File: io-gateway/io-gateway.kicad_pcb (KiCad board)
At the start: 4 copper layers, 155 x 81.5 mm, 117 parts, among them IC1 MAX17673AATI+, J1 1752201, J2 1752201, J3 1752201, J4 Screw_Terminal_01x09, J5 Screw_Terminal_01x09, J6 Screw_Terminal_01x09, K1 2071556-2, K2 2071556-2, K3 2071556-2, K4 2071556-2, K5 2071556-2, K6 2071556-2, K7 2071556-2, K9 2071556-2, Q1 NTR4003NT1G, Q2 NTR4003NT1G, Q3 NTR4003NT1G, Q4 NTR4003NT1G, Q5 NTR4003NT1G, Q6 NTR4003NT1G, Q7 NTR4003NT1G, Q9 NTR4003NT1G, U1 LED5000, U2 LED5000

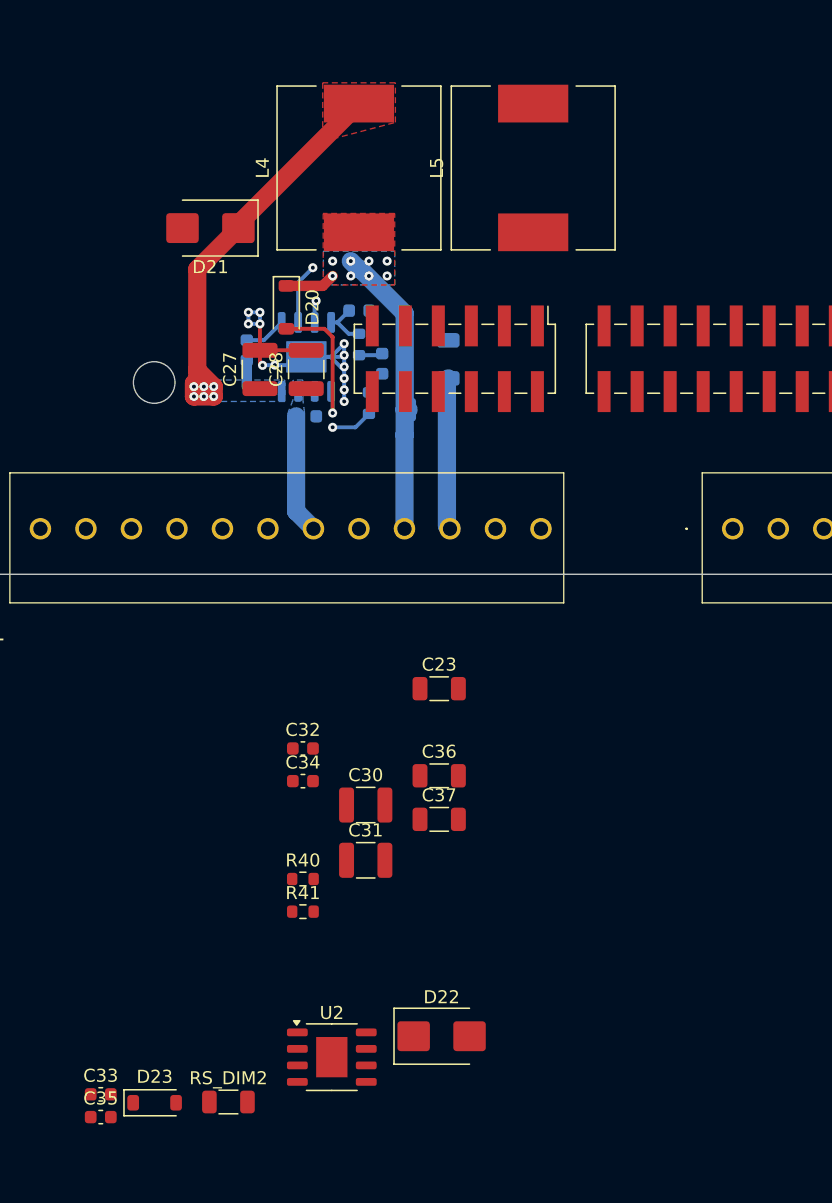
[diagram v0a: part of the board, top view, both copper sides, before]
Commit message: add second dimmer
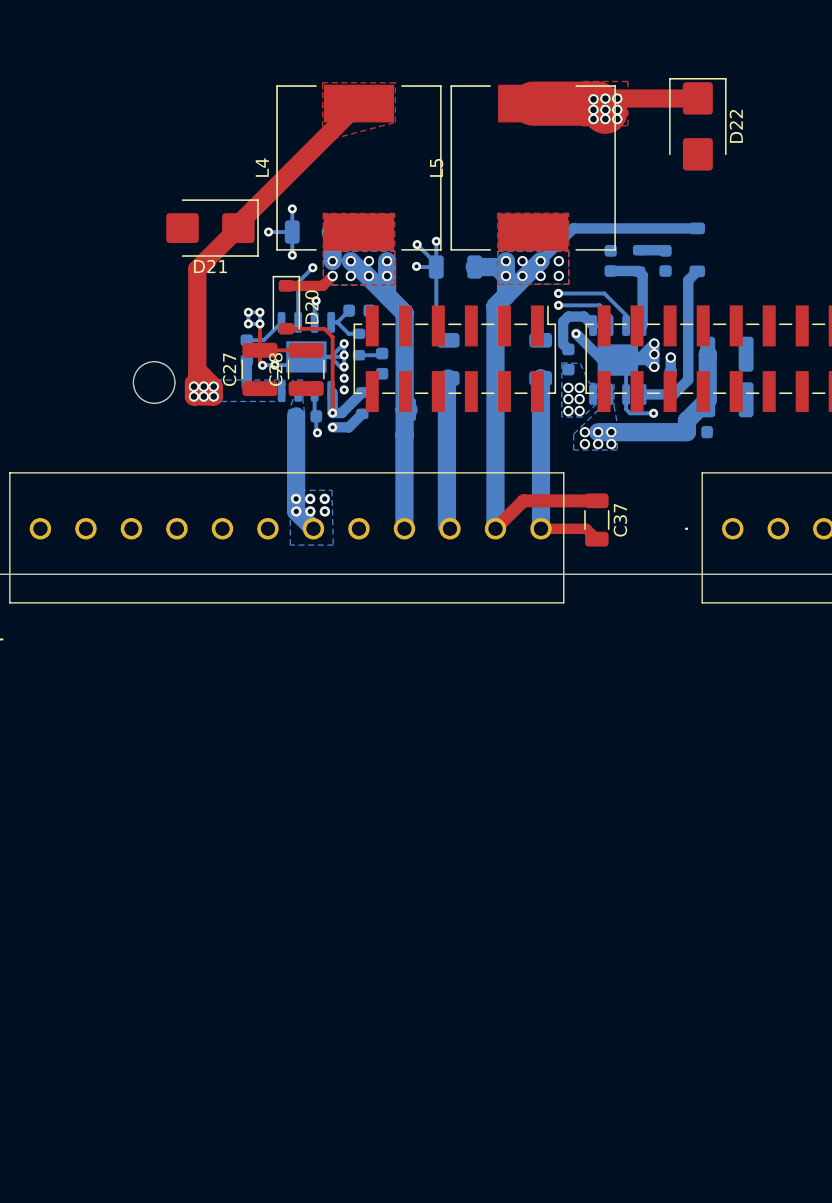
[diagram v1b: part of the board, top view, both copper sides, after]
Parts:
- C23, C30, C31, C32, C33, C34, C35, C36, D23, R40, R41, RS_DIM2, U2: moved to B.Cu
- moved D23 77.7 mm to (105.8, 104.8), turned to -90 degrees
- moved D22 72.7 mm to (105.8, 95.3), turned to -90 degrees
- moved C33 68.5 mm to (105.8, 118.8)
- moved C35 68.5 mm to (95.9, 113.2), turned to -90 degrees
- moved RS_DIM2 62.0 mm to (93.7, 113.2), turned to 90 degrees
- moved U2 58.0 mm to (99.7, 113.3), turned to -90 degrees
- moved R40 54.1 mm to (101.3, 105.7), turned to -90 degrees
- moved R41 49.5 mm to (103.7, 115.1), turned to -90 degrees
- moved C31 47.8 mm to (108.1, 112.8)
- moved C32 46.7 mm to (103.3, 105.7), turned to -90 degrees
- moved C34 46.5 mm to (99.1, 105.7), turned to 90 degrees
- moved C30 41.8 mm to (108.0, 116.3)
- moved C36 39.1 mm to (87.2, 106.1), turned to 180 degrees
- moved C23 36.5 mm to (76.1, 103.4), turned to 180 degrees
- moved C37 26.0 mm to (98.0, 125.6), turned to -90 degrees
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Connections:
- net Net-(D22-K) renamed /Dimmer1/DIM2_SW
- net Net-(D23-A) renamed /Dimmer1/DIM2_FB
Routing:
- net DIM2_VLED_VCC: track 0.00 -> 50.3 mm, vias 0 -> 8
- net VIN_DIM1: track 9.20 -> 49.3 mm, vias 0 -> 12
- net /Dimmer1/DIM2_SW: track 0.00 -> 37.2 mm, vias 0 -> 15
- net GND_CTRL: track 27.8 -> 64.4 mm, vias 12 -> 23
- net DIM2_VLED_GND: track 0.00 -> 35.8 mm, vias 0 -> 1
- net /Dimmer1/DIM2_FB: track 0.00 -> 12.6 mm
- net DIM1_VLED_VCC: track 26.6 -> 33.4 mm
- net INH_DIM2: track 0.00 -> 6.69 mm, vias 0 -> 1
- net Net-(U2-COMP): track 0.00 -> 6.46 mm
- net Net-(U2-BOOT): track 0.00 -> 5.10 mm
- net PWM_DIM2: track 0.00 -> 5.04 mm, vias 0 -> 1
- net /Dimmer1/DIM1_FB: track 11.4 -> 14.3 mm
- net DIM1_VLED_GND: track 28.7 -> 26.7 mm
- net Net-(C32-Pad1): track 0.00 -> 2.05 mm
- added copper zone on B.Cu, net /Dimmer1/DIM2_SW
- added copper zone on F.Cu, net /Dimmer1/DIM2_SW
- added copper zone on In2.Cu, net /Dimmer1/DIM2_SW
- added copper zone on B.Cu, net DIM2_VLED_VCC
- added copper zone on F.Cu, net DIM2_VLED_VCC
- added copper zone on In2.Cu, net VIN_DIM1

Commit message: add voltage regulator
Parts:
- removed C1, C4, C5: 22µF, Capacitor_SMD:C_0603_1608Metric
- removed C10, C13, C9: 2.2µF, Capacitor_SMD:C_0603_1608Metric
- removed C11: 47µF, Capacitor_SMD:C_0603_1608Metric
- removed C12: 1µF, Capacitor_SMD:C_0603_1608Metric
- removed C14, C16, C20, C21, C7: 100nF, Capacitor_SMD:C_0603_1608Metric
- removed C15: 4.7µF, Capacitor_SMD:CP_Elec_4x5.4
- removed C17, C2, C3, C6, C8: open, Capacitor_SMD:C_0603_1608Metric
- removed C18: 47µF, Capacitor_SMD:CP_Elec_6.3x5.4
- removed C19: 4.7µF, Capacitor_SMD:C_0603_1608Metric
- removed IC1: MAX17673AATI+, Package_DFN_QFN:QFN50P500X500X80-29N
- removed JP1, JP2: Jumper_2_Bridged, TestPoint:TestPoint_2Pads_Pitch2.54mm_Drill0.8mm
- removed L1: 1.5µH, Inductor_SMD:L_1210_3225Metric
- removed L2: 22µH, Inductor_SMD:L_1008_2520Metric
- removed L3: 2.2µH, Inductor_SMD:L_1210_3225Metric
- removed R1: 12K, Resistor_SMD:R_0201_0603Metric
- removed R11: 100R, Resistor_SMD:R_0201_0603Metric
- removed R12, R3: 10K, Resistor_SMD:R_0201_0603Metric
- removed R14: 470K, Resistor_SMD:R_0201_0603Metric
- removed R15, R8: 22K, Resistor_SMD:R_0201_0603Metric
- removed R16, R18, R19, R20: open, Resistor_SMD:R_0201_0603Metric
- removed R17, R21: 0R, Resistor_SMD:R_0201_0603Metric
- removed R2: 68K, Resistor_SMD:R_0201_0603Metric
- removed R4: 3K3, Resistor_SMD:R_0201_0603Metric
- removed R5: 330k, Resistor_SMD:R_0201_0603Metric
- removed R6: 1M, Resistor_SMD:R_0201_0603Metric
- removed R7: 1R, Resistor_SMD:R_0201_0603Metric
- removed R9: 33K, Resistor_SMD:R_0201_0603Metric
- added C38: 10µF 50V, Capacitor_SMD:C_1210_3225Metric, B.Cu at (56.9, 89.9)
- added C39: 100nF 50V, Capacitor_SMD:C_0603_1608Metric, B.Cu at (55.5, 87.4)
- added C40: 100nF 50V, Capacitor_SMD:C_0603_1608Metric, B.Cu at (55.8, 78.7)
- added C41: 22µF, Capacitor_SMD:C_0603_1608Metric, B.Cu at (64.3, 72.8)
- added C42: 22µF, Capacitor_SMD:C_0603_1608Metric, B.Cu at (60.8, 72.8)
- added C43: 75pF, Capacitor_SMD:C_0603_1608Metric, B.Cu at (53.2, 79.2)
- added C44: 47µF, Capacitor_SMD:CP_Elec_6.3x5.4, F.Cu at (56.9, 83.1)
- added L6: 10µF, Inductor_THT:L_Radial_D7.5mm_P3.50mm_Fastron_07P, F.Cu at (56.5, 75.4)
- added R27: 470k, Resistor_SMD:R_0603_1608Metric, F.Cu at (61.0, 88.3)
- added R29: 100k, Resistor_SMD:R_0603_1608Metric, F.Cu at (61.7, 91.2)
- added R30: 49.9, Resistor_SMD:R_0603_1608Metric, B.Cu at (53.0, 72.9)
- added R31: 100k, Resistor_SMD:R_0603_1608Metric, B.Cu at (53.2, 76.2)
- added R32: 10k, Resistor_SMD:R_0603_1608Metric, B.Cu at (53.0, 85.6)
- added R33: 3k3, Resistor_SMD:R_0603_1608Metric, B.Cu at (53.0, 89.9)
- added U3: TPS54308, Package_TO_SOT_SMD:SOT-23-6, B.Cu at (56.9, 83.8)
- moved FRDM_MCXA153_1 111.1 mm to (183.9, 110.0), turned to 180 degrees
- moved D1 47.8 mm to (55.2, 90.2), turned to 180 degrees
- moved F1 24.3 mm to (56.0, 105.7)
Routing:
- net +5V: track 0.00 -> 133.3 mm, vias 0 -> 6
- net Net-(U3-EN): track 0.00 -> 19.7 mm, vias 0 -> 2
- net +24V: track 0.00 -> 16.2 mm, vias 0 -> 4
- net /MCU_VoltageRegulator/VregSW: track 0.00 -> 15.0 mm
- net VDC_CTRL: track 0.00 -> 12.4 mm
- net /MCU_VoltageRegulator/VregFB: track 0.00 -> 11.9 mm
- net Net-(C43-Pad1): track 0.00 -> 5.77 mm
- net Net-(U3-BOOT): track 0.00 -> 3.30 mm
- net Net-(R32-Pad2): track 0.00 -> 2.67 mm
- net GND_CTRL: vias 23 -> 28
- added copper zone on B.Cu, net +24V
- added copper zone on F.Cu, net +24V
- added copper zone on B.Cu, net /MCU_VoltageRegulator/VregSW
- added copper zone on B.Cu, net GND_CTRL
- added copper zone on F.Cu, net unconnected-(FRDM_MCXA153_1B-Pin_J3_16_VIN-Pad3.16)

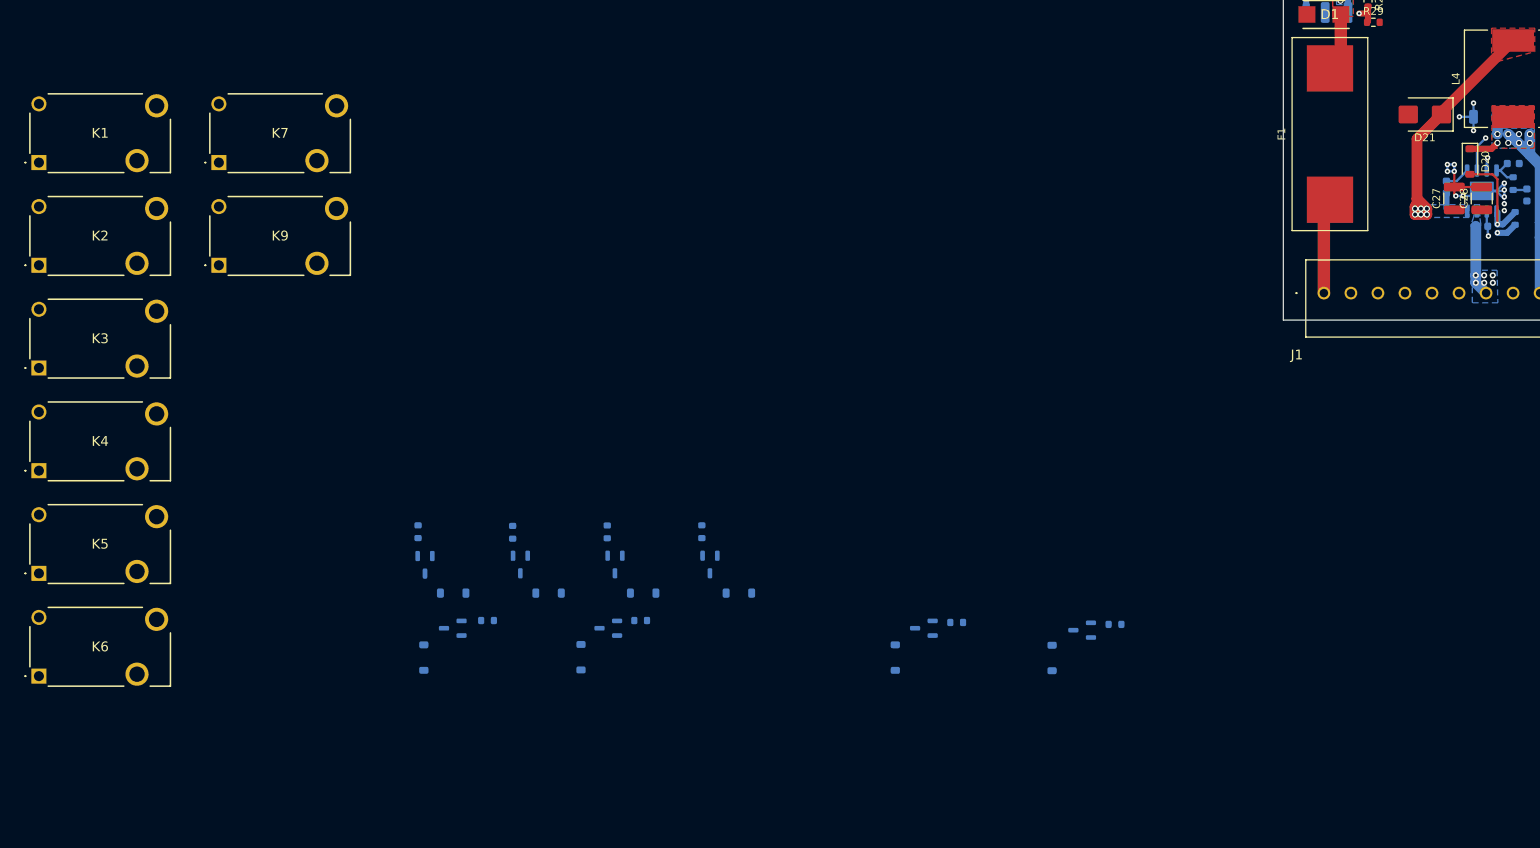
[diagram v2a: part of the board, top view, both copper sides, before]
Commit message: reannotate dimmers and relays
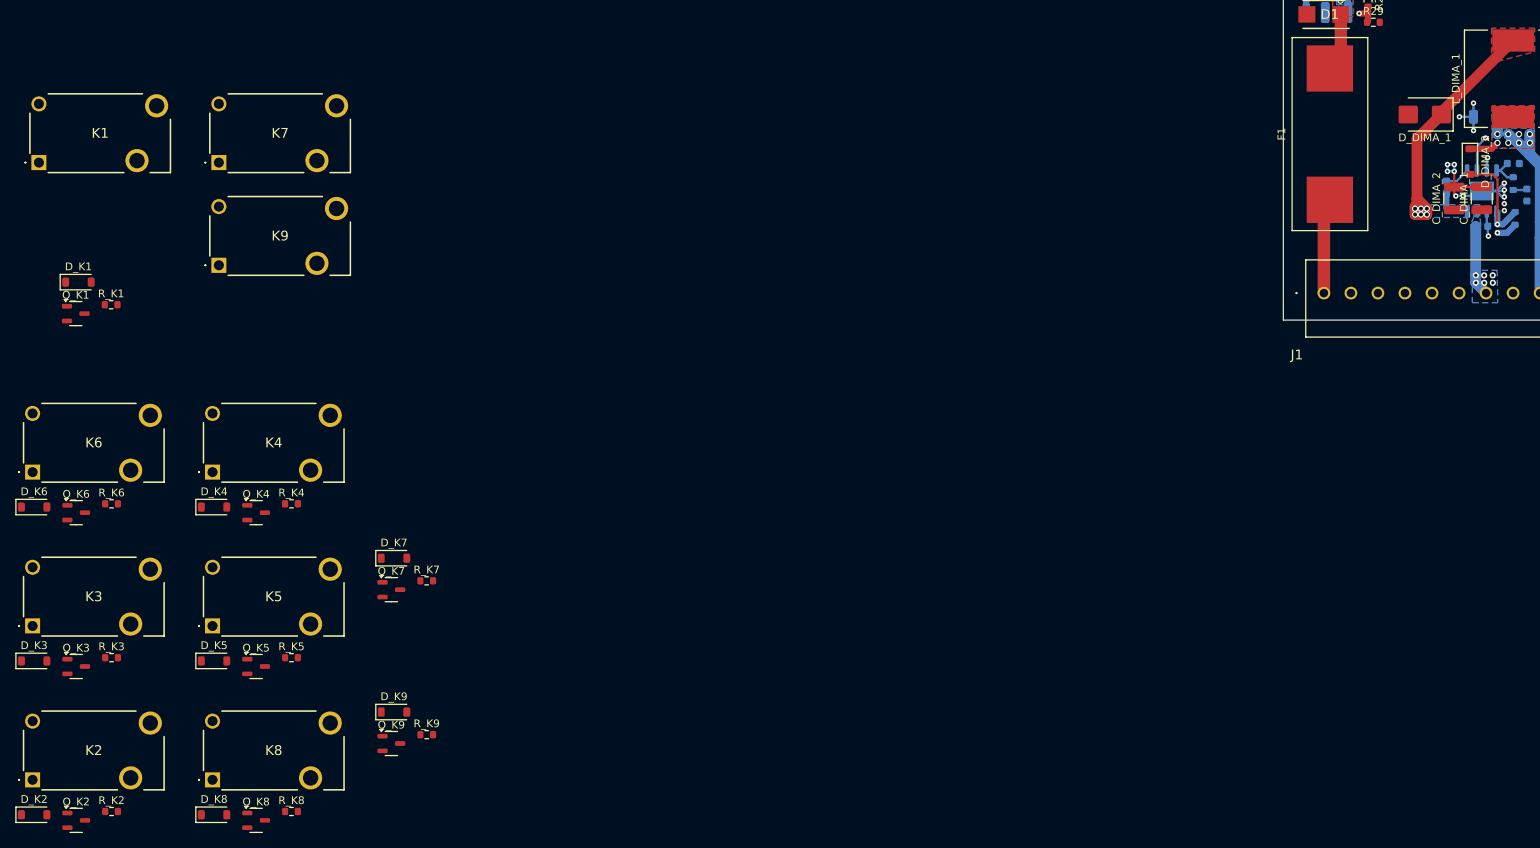
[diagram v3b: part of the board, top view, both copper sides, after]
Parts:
- removed D10, D2, D3, D4, D5, D6, D7, D8: MMSD914, Diode_SMD:D_SOD-123
- removed Q1, Q2, Q3, Q4, Q5, Q6, Q7, Q9: NTR4003NT1G, Package_TO_SOT_SMD:SOT-23-3
- removed R10, R13, R22, R23, R24, R25, R26, R28: 100, Resistor_SMD:R_0603_1608Metric
- added D_K1: MMSD914, Diode_SMD:D_SOD-123, F.Cu at (-106.0, 124.8)
- added D_K2: MMSD914, Diode_SMD:D_SOD-123, F.Cu at (-111.8, 193.8)
- added D_K3: MMSD914, Diode_SMD:D_SOD-123, F.Cu at (-111.8, 173.9)
- added D_K4: MMSD914, Diode_SMD:D_SOD-123, F.Cu at (-88.5, 154.0)
- added D_K5: MMSD914, Diode_SMD:D_SOD-123, F.Cu at (-88.5, 173.9)
- added D_K6: MMSD914, Diode_SMD:D_SOD-123, F.Cu at (-111.8, 154.0)
- added D_K7: MMSD914, Diode_SMD:D_SOD-123, F.Cu at (-65.2, 160.6)
- added D_K8: MMSD914, Diode_SMD:D_SOD-123, F.Cu at (-88.5, 193.8)
- added D_K9: MMSD914, Diode_SMD:D_SOD-123, F.Cu at (-65.2, 180.5)
- added K8: 2071556-2, Relay:20715562, F.Cu at (-88.7, 189.3)
- added Q_K1: NTR4003NT1G, Package_TO_SOT_SMD:SOT-23-3, F.Cu at (-106.4, 128.9)
- added Q_K2: NTR4003NT1G, Package_TO_SOT_SMD:SOT-23-3, F.Cu at (-106.3, 194.5)
- added Q_K3: NTR4003NT1G, Package_TO_SOT_SMD:SOT-23-3, F.Cu at (-106.3, 174.6)
- added Q_K4: NTR4003NT1G, Package_TO_SOT_SMD:SOT-23-3, F.Cu at (-83.0, 154.7)
- added Q_K5: NTR4003NT1G, Package_TO_SOT_SMD:SOT-23-3, F.Cu at (-83.0, 174.6)
- added Q_K6: NTR4003NT1G, Package_TO_SOT_SMD:SOT-23-3, F.Cu at (-106.3, 154.7)
- added Q_K7: NTR4003NT1G, Package_TO_SOT_SMD:SOT-23-3, F.Cu at (-65.5, 164.7)
- added Q_K8: NTR4003NT1G, Package_TO_SOT_SMD:SOT-23-3, F.Cu at (-83.0, 194.5)
- added Q_K9: NTR4003NT1G, Package_TO_SOT_SMD:SOT-23-3, F.Cu at (-65.5, 184.6)
- added R_K1: 100, Resistor_SMD:R_0603_1608Metric, F.Cu at (-101.8, 127.8)
- added R_K2: 100, Resistor_SMD:R_0603_1608Metric, F.Cu at (-101.7, 193.4)
- added R_K3: 100, Resistor_SMD:R_0603_1608Metric, F.Cu at (-101.7, 173.5)
- added R_K4: 100, Resistor_SMD:R_0603_1608Metric, F.Cu at (-78.4, 153.5)
- added R_K5: 100, Resistor_SMD:R_0603_1608Metric, F.Cu at (-78.4, 173.5)
- added R_K6: 100, Resistor_SMD:R_0603_1608Metric, F.Cu at (-101.7, 153.5)
- added R_K7: 100, Resistor_SMD:R_0603_1608Metric, F.Cu at (-60.9, 163.5)
- added R_K8: 100, Resistor_SMD:R_0603_1608Metric, F.Cu at (-78.4, 193.4)
- added R_K9: 100, Resistor_SMD:R_0603_1608Metric, F.Cu at (-60.9, 183.4)
- moved K2 66.6 mm to (-112.0, 189.3)
- moved K3 33.4 mm to (-112.0, 169.4)
- moved K6 26.4 mm to (-112.0, 149.4)
- moved K5 23.5 mm to (-88.7, 169.4)
- moved K4 22.5 mm to (-88.7, 149.4)
- renumbered C28 to C_DIMA_1, C27 to C_DIMA_2, C29 to C_DIMA_3, C26 to C_DIMA_4, C25 to C_DIMA_5, C22 to C_DIMA_6, C23 to C_DIMA_7, C24 to C_DIMA_8, D21 to D_DIMA_1, D20 to D_DIMA_2, L4 to L_DIMA_1, RS_DIM1 to RS_DIMA_1, R39 to R_DIMA_1, R38 to R_DIMA_2, U1 to U_DIMA1, U2 to U_DIMB1
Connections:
- net INH_DIM1 renamed /Dimmer1/INH_DIMA
- net INH_DIM2 renamed /Dimmer1/INH_DIMB
- net PWM_DIM2 renamed /Dimmer1/PWM_DIMB
- net VAC_IN_1 renamed /VAC_IN_1
- net VAC_IN_2 renamed /VAC_IN_2
- net VAC_IN_3 renamed /VAC_IN_3
- net VAC_IN_4 renamed /Relay4/VAC_IN
- net VAC_IN_5 renamed /Relay5/VAC_IN
- net VAC_IN_6 renamed /Relay6/VAC_IN
- net VAC_IN_7 renamed /Relay7/VAC_IN
- net VAC_OUT_1 renamed /VAC_OUT_1.1
- net VAC_OUT_2 renamed /VAC_OUT_2.1
- net VAC_OUT_3 renamed /VAC_OUT_3.1
- net VAC_OUT_4 renamed /Relay4/VAC_OUT
- net VAC_OUT_5 renamed /Relay5/VAC_OUT
- net VAC_OUT_6 renamed /Relay6/VAC_OUT
- net VAC_OUT_7 renamed /Relay7/VAC_OUT
- net VIN_DIM1 renamed /Dimmer1/VIN_DIM
- J6 pad 4: VAC_IN_8 -> /Relay8/VAC_IN
- J6 pad 5: VAC_OUT_8 -> /Relay8/VAC_OUT
- J6 pad 7: VAC_IN_9 -> /Relay9/VAC_IN
- J6 pad 8: VAC_OUT_9 -> /Relay9/VAC_OUT
- K9 pad 3: VAC_OUT_8 -> /Relay9/VAC_OUT
- K9 pad 4: VAC_IN_8 -> /Relay9/VAC_IN
- U_DIMA1 pad 2: PWM_DIM1 -> /Dimmer1/PWM_DIMA
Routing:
- net PWM_DIM1: track 4.68 -> 0.00 mm, vias 1 -> 0
- net /Dimmer1/PWM_DIMA: track 0.00 -> 4.68 mm, vias 0 -> 1

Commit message: temp
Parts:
- added C_DIMA_10: 10µF 50V, Capacitor_SMD:C_1210_3225Metric, F.Cu at (146.5, 270.2)
- added C_DIMA_11: 470pF, Capacitor_SMD:C_0603_1608Metric, F.Cu at (145.7, 282.1)
- added C_DIMA_12: 100nF 50V, Capacitor_SMD:C_0603_1608Metric, F.Cu at (145.7, 284.6)
- added C_DIMA_13: 22pF, Capacitor_SMD:C_0603_1608Metric, F.Cu at (145.7, 287.1)
- added C_DIMA_14: 100nF 50V, Capacitor_SMD:C_0603_1608Metric, F.Cu at (145.7, 289.6)
- added C_DIMA_15: 1µF 50V, Capacitor_SMD:C_1206_3216Metric, F.Cu at (152.1, 265.5)
- added C_DIMA_16: NM, Capacitor_SMD:C_1206_3216Metric, F.Cu at (152.1, 268.9)
- added C_DIMA_9: 10µF 50V, Capacitor_SMD:C_1210_3225Metric, F.Cu at (146.5, 266.0)
- added C_DIMB_10: 10µF 50V, Capacitor_SMD:C_1210_3225Metric, F.Cu at (146.5, 278.7)
- added C_DIMB_11: 470pF, Capacitor_SMD:C_0603_1608Metric, F.Cu at (149.7, 282.1)
- added C_DIMB_12: 100nF 50V, Capacitor_SMD:C_0603_1608Metric, F.Cu at (149.7, 284.6)
- added C_DIMB_13: 22pF, Capacitor_SMD:C_0603_1608Metric, F.Cu at (149.7, 287.1)
- added C_DIMB_14: 100nF 50V, Capacitor_SMD:C_0603_1608Metric, F.Cu at (149.7, 289.6)
- added C_DIMB_15: 1µF 50V, Capacitor_SMD:C_1206_3216Metric, F.Cu at (152.1, 272.2)
- added C_DIMB_16: NM, Capacitor_SMD:C_1206_3216Metric, F.Cu at (152.1, 275.6)
- added C_DIMB_9: 10µF 50V, Capacitor_SMD:C_1210_3225Metric, F.Cu at (146.5, 274.5)
- added D_DIMA_3: D_Schottky, Diode_SMD:D_SMB, F.Cu at (159.9, 283.6)
- added D_DIMA_4: D_Zener, Diode_SMD:D_SOD-123, F.Cu at (146.6, 292.6)
- added D_DIMB_3: D_Schottky, Diode_SMD:D_SMB, F.Cu at (159.9, 289.2)
- added D_DIMB_4: D_Zener, Diode_SMD:D_SOD-123, F.Cu at (146.6, 295.9)
- added L_DIMA_2: 47µH 3.8A, Inductor_SMD:L_12x12mm_H8mm, F.Cu at (136.3, 271.0)
- added L_DIMB_2: 47µH 3.8A, Inductor_SMD:L_12x12mm_H8mm, F.Cu at (136.3, 285.2)
- added RS_DIMA_2: R, Resistor_SMD:R_1206_3216Metric, F.Cu at (152.2, 292.5)
- added RS_DIMB_2: R, Resistor_SMD:R_1206_3216Metric, F.Cu at (152.2, 295.9)
- added R_DIMA_3: 24k9, Resistor_SMD:R_0603_1608Metric, F.Cu at (153.7, 282.1)
- added R_DIMA_4: 47k, Resistor_SMD:R_0603_1608Metric, F.Cu at (153.7, 284.6)
- added R_DIMB_3: 24k9, Resistor_SMD:R_0603_1608Metric, F.Cu at (153.7, 287.1)
- added R_DIMB_4: 47k, Resistor_SMD:R_0603_1608Metric, F.Cu at (153.7, 289.6)
- added U_DIMA2: LED5000, Package_SO:HSOP-8-1EP_3.9x4.9mm_P1.27mm_EP2.41x3.1mm, F.Cu at (159.2, 267.2)
- added U_DIMB2: LED5000, Package_SO:HSOP-8-1EP_3.9x4.9mm_P1.27mm_EP2.41x3.1mm, F.Cu at (159.2, 273.8)
- renumbered C30 to C_DIMB_1, C31 to C_DIMB_2, C33 to C_DIMB_3, C32 to C_DIMB_4, C34 to C_DIMB_5, C35 to C_DIMB_6, C36 to C_DIMB_7, C37 to C_DIMB_8, D22 to D_DIMB_1, D23 to D_DIMB_2, L5 to L_DIMB_1, RS_DIM2 to RS_DIMB_1, R40 to R_DIMB_1, R41 to R_DIMB_2
